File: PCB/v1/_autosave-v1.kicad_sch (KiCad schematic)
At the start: 80 parts, among them J1 Screw_Terminal_01x02, Q2 BC548, SW1 Push Button, SW2 Push Button, U1 4060, U10 7400, U2 4060, U3 CD4026BE, U4 CD4026BE, U5 CD4026BE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

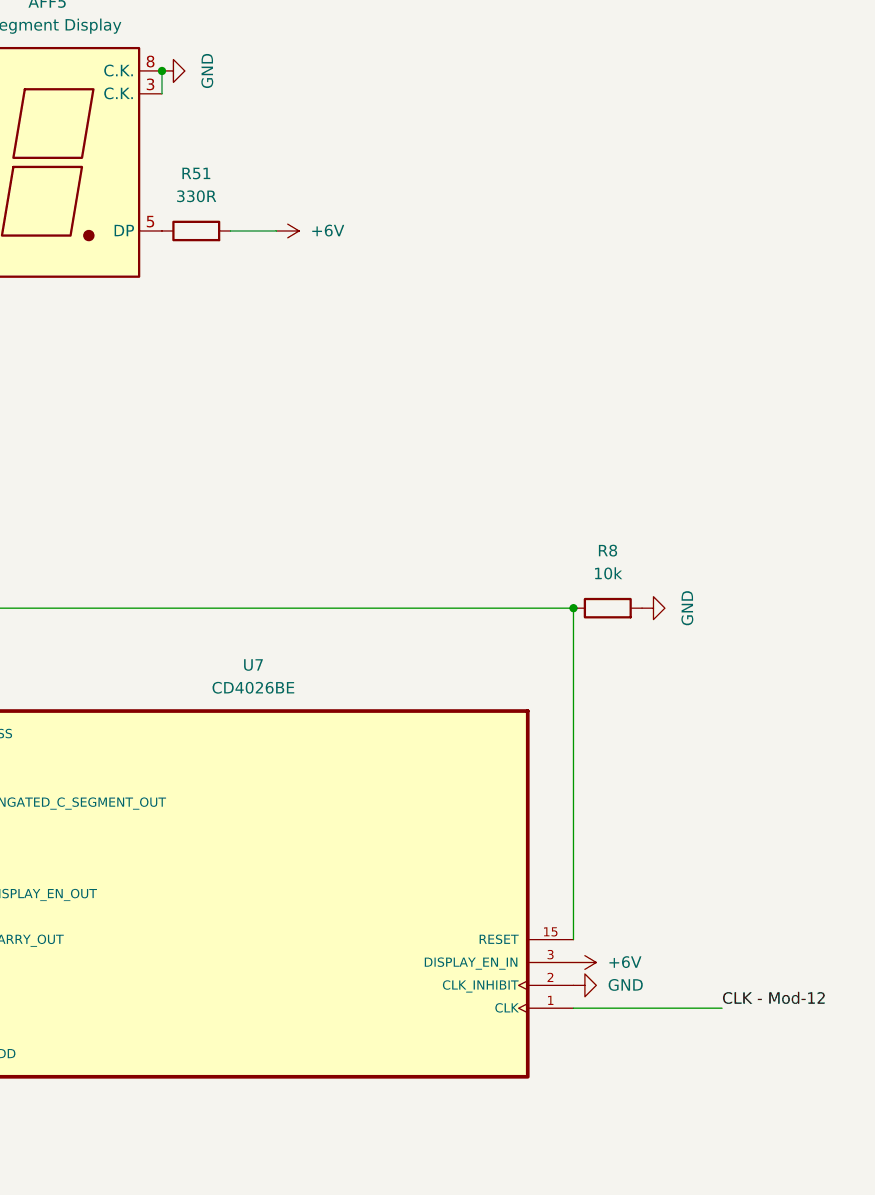
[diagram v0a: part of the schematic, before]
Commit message: Updated Schematic, made PCB Design
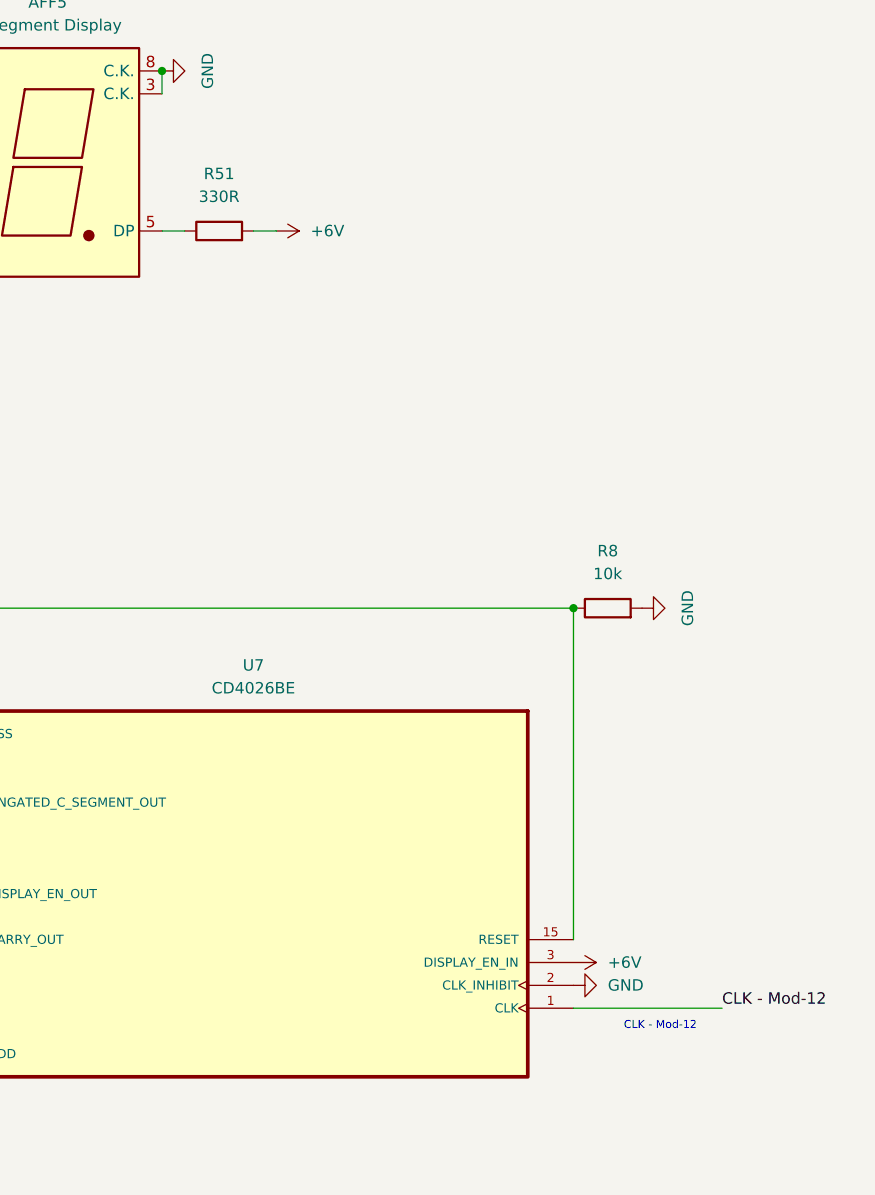
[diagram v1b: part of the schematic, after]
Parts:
- U10: footprint Package_DIP:SMDIP-14_W7.62mm -> Package_DIP:DIP-14_W10.16mm
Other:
- note added: "CLK - Mod-12"
- moved on the sheet: R51
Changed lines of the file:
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@@
 		)
 	)
+	(text "CLK - Mod-12"
+		(exclude_from_sim no)
+		(at 356.362 316.992 0)
+		(effects
+			(font
+				(size 0.889 0.889)
+				(color 0 0 0 1)
+			)
+		)
+	)
 	(text "Power Supply"
 		(exclude_from_sim no)
@@
 	(wire
 		(pts
-			(xy 308.61 228.6) (xy 313.69 228.6)
+			(xy 311.15 228.6) (xy 313.69 228.6)
 		)
 		(stroke
@@
 	(wire
 		(pts
+			(xy 300.99 228.6) (xy 303.53 228.6)
+		)
+		(stroke
+			(width 0)
+			(type default)
+		)
+	)
+	(wire
+		(pts
 			(xy 106.68 210.82) (xy 116.84 210.82)
 		)
@@
 			)
 		)
-		(property "Footprint" "Package_DIP:SMDIP-14_W7.62mm"
+		(property "Footprint" "Package_DIP:DIP-14_W10.16mm"
 			(at 153.67 132.08 0)
 			(effects
@@
 			)
 		)
-		(property "Footprint" "Package_DIP:SMDIP-14_W7.62mm"
+		(property "Footprint" "Package_DIP:DIP-14_W10.16mm"
 			(at 180.34 132.08 0)
 			(effects
@@
 	(symbol
 		(lib_id "Device:R")
-		(at 304.8 228.6 90)
+		(at 307.34 228.6 90)
 		(unit 1)
 		(exclude_from_sim no)
@@
 		(fields_autoplaced yes)
 		(property "Reference" "R51"
-			(at 304.8 222.25 90)
+			(at 307.34 222.25 90)
 			(effects
 				(font
@@
 		)
 		(property "Value" "330R"
-			(at 304.8 224.79 90)
+			(at 307.34 224.79 90)
 			(effects
 				(font
@@
 		)
 		(property "Footprint" "Resistor_SMD:R_0805_2012Metric"
-			(at 304.8 230.378 90)
+			(at 307.34 230.378 90)
 			(effects
 				(font
@@
 		)
 		(property "Datasheet" "~"
-			(at 304.8 228.6 0)
+			(at 307.34 228.6 0)
 			(effects
 				(font
@@
 		)
 		(property "Description" "Resistor"
-			(at 304.8 228.6 0)
+			(at 307.34 228.6 0)
 			(effects
 				(font
@@
 			)
 		)
-		(property "Footprint" "Package_DIP:SMDIP-14_W7.62mm"
+		(property "Footprint" "Package_DIP:DIP-14_W10.16mm"
 			(at 130.81 132.08 0)
 			(effects
@@
 			)
 		)
-		(property "Footprint" "Package_DIP:SMDIP-14_W7.62mm"
+		(property "Footprint" "Package_DIP:DIP-14_W10.16mm"
 			(at 110.49 129.54 0)
 			(effects
